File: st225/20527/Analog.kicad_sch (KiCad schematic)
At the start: 111 parts, among them J1 control, J2 data, J4 SPINDLE, J5 HEADS, J7 CONFIG, Q1 BD436, Q2 2N6039, Q3 BD436, Q4 2N6039, Q5 BD436, Q7 2N3906, Q9 2N3906

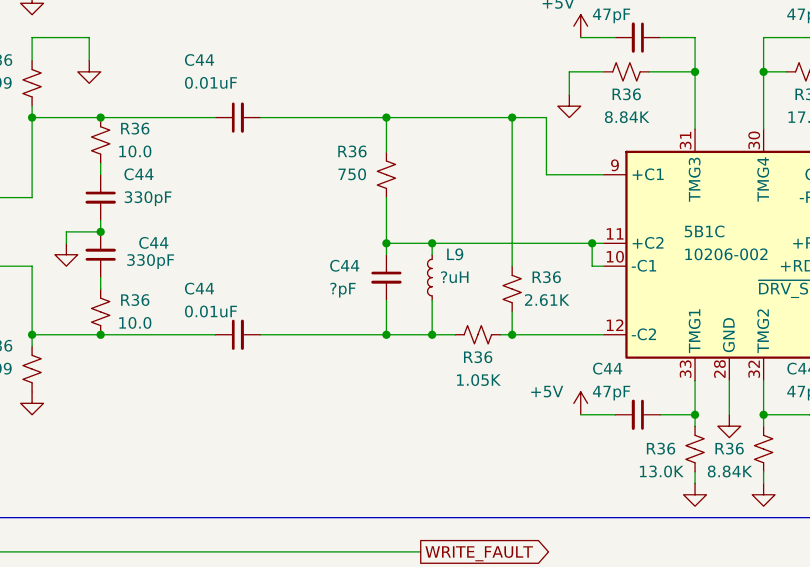
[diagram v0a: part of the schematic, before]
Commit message: Add some part values to 20527
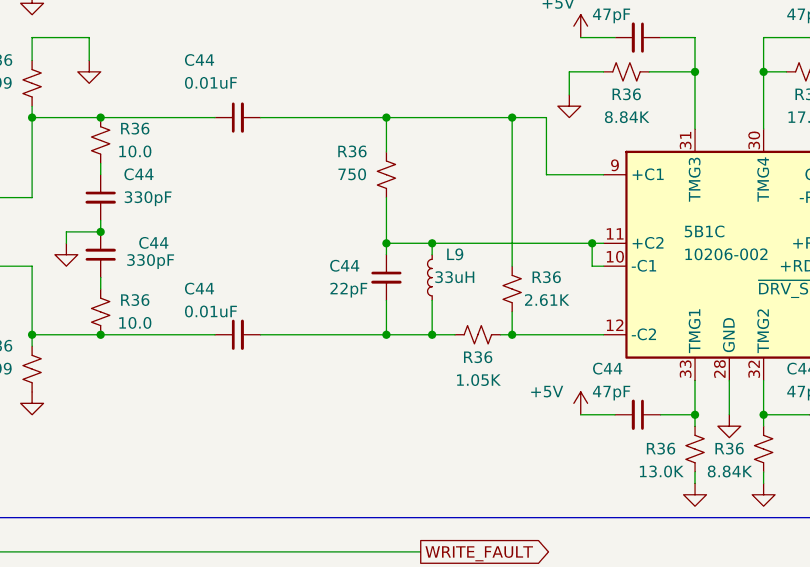
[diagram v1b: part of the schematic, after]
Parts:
- C44: value ?pF -> 22pF
- L9: value ?uH -> 33uH
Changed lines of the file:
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@@
       (effects (font (size 1.27 1.27)) (justify left))
     )
-    (property "Value" "?pF" (at 326.39 87.63 0)
+    (property "Value" "22pF" (at 326.39 87.63 0)
       (effects (font (size 1.27 1.27)) (justify left))
     )
@@
       (effects (font (size 1.27 1.27)))
     )
-    (property "Value" "?uH" (at 340.36 86.36 0)
-      (effects (font (size 1.27 1.27)))
-    )
+    (property "Value" "33uH" (at 340.36 86.36 0)
+      (effects (font (size 1.27 1.27)))
+    )
